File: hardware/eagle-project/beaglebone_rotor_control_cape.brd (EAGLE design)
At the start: 71.8 x 54.6 mm, 57 parts, among them IC1 TLC2264CDU, IC2 MCP4901, IC3 MAX3232ESE, IC4 TLC2264CDU, IC5 MCP4901, IC6 TLC2264CDU, Q1 SQ2348ES-T1-GE3, Q2 SQ2348ES-T1-GE3, Q3 SQ2348ES-T1-GE3, Q4 SQ2348ES-T1-GE3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

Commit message: * layout: added spi1 and determined pin for usb slave turn on
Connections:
- removed net N$23: R25.1
- removed net N$24: R24.1
- removed net N$26: R23.1
- new net BB_SPI1_CS0: R25.1, X1.74
- new net BB_SPI1_D0: R23.1, X1.75
- new net BB_SPI1_D1: X1.76
- new net BB_SPI1_SCLK: R24.1, X1.77
- new net BB_USB_VCC: X1.18
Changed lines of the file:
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@@
 <contactref element="R21" pad="1"/>
-</signal>
-<signal name="N$23">
-<contactref element="R25" pad="1"/>
-</signal>
-<signal name="N$24">
-<contactref element="R24" pad="1"/>
-</signal>
-<signal name="N$26">
-<contactref element="R23" pad="1"/>
 </signal>
 <signal name="N$27">
@@
 <contactref element="Q3" pad="3"/>
 </signal>
+<signal name="BB_USB_VCC">
+<contactref element="X1" pad="18"/>
+</signal>
+<signal name="BB_SPI1_CS0">
+<contactref element="X1" pad="74"/>
+<contactref element="R25" pad="1"/>
+<wire x1="-20.635" y1="-287.02" x2="35.56" y2="51.435" width="0" layer="19" extent="1-1"/>
+</signal>
+<signal name="BB_SPI1_SCLK">
+<contactref element="X1" pad="77"/>
+<contactref element="R24" pad="1"/>
+<wire x1="-20.635" y1="-280.67" x2="30.48" y2="53.975" width="0" layer="19" extent="1-1"/>
+</signal>
+<signal name="BB_SPI1_D1">
+<contactref element="X1" pad="76"/>
+</signal>
+<signal name="BB_SPI1_D0">
+<contactref element="X1" pad="75"/>
+<contactref element="R23" pad="1"/>
+<wire x1="-20.635" y1="-274.32" x2="33.02" y2="53.975" width="0" layer="19" extent="1-1"/>
+</signal>
 </signals>

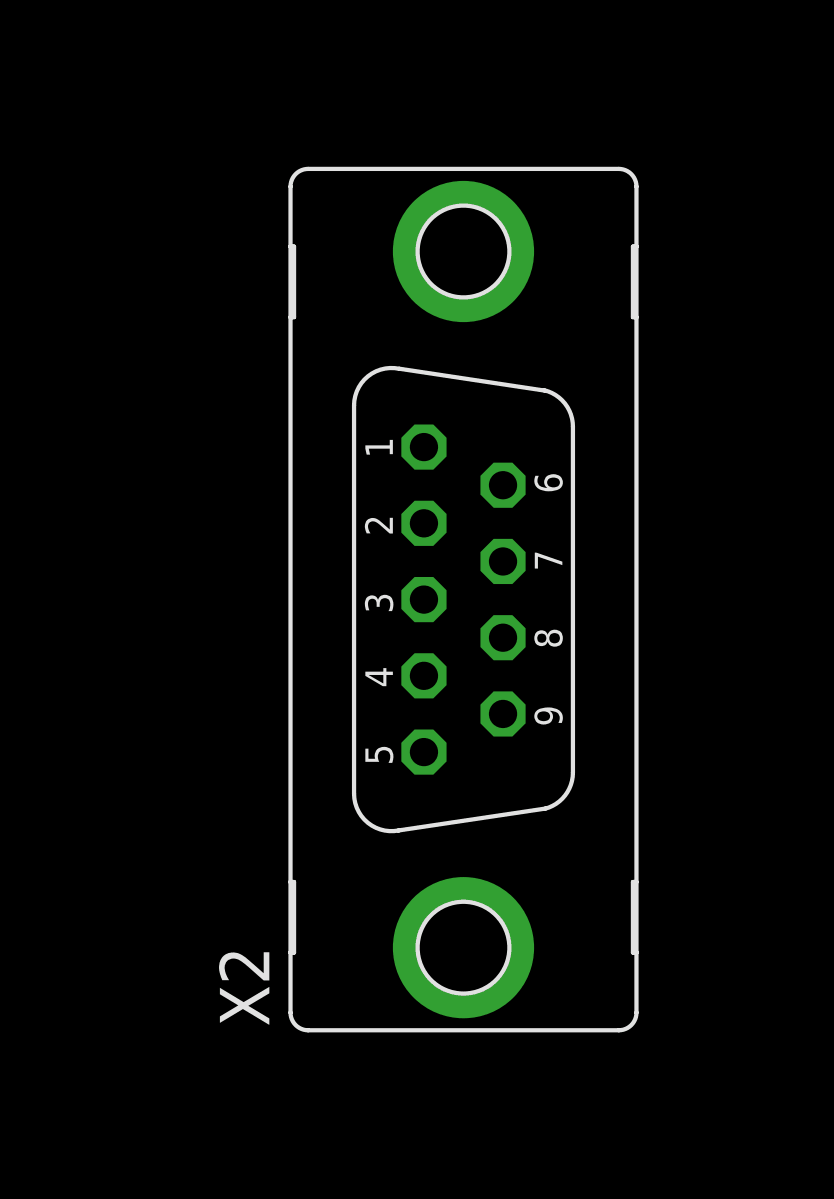
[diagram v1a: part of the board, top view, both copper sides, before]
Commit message: Created library for D-Sub connector from TE.com
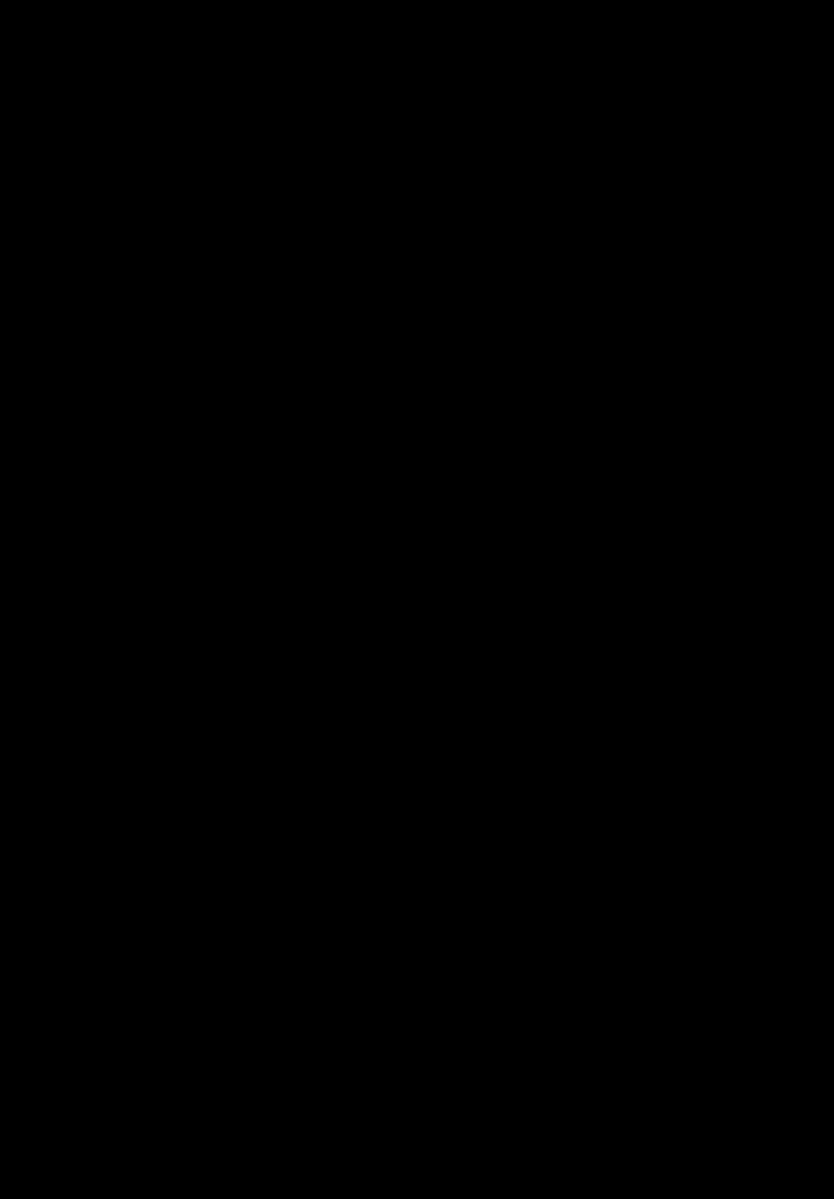
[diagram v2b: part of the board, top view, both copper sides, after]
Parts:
- removed X2: (no value), con-subd:F09VP
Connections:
- net GND: no longer X2.5
- net RS232_RX: no longer X2.3
- net RS232_TX: no longer X2.2
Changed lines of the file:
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@@
 <element name="R8" library="rcl" package="R0805" value="100" x="61.595" y="43.18" rot="R270"/>
 <element name="R1" library="rcl" package="R0805" value="100" x="59.055" y="43.18" rot="R270"/>
-<element name="X2" library="con-subd" package="F09VP" value="" x="6.35" y="-123.19" rot="R90">
-<attribute name="OC_NEWARK" value="unknown" x="6.35" y="-123.19" size="1.778" layer="27" rot="R90" display="off"/>
-<attribute name="MPN" value="" x="6.35" y="-123.19" size="1.778" layer="27" rot="R90" display="off"/>
-<attribute name="MF" value="" x="6.35" y="-123.19" size="1.778" layer="27" rot="R90" display="off"/>
-<attribute name="OC_FARNELL" value="unknown" x="6.35" y="-123.19" size="1.778" layer="27" rot="R90" display="off"/>
-</element>
 <element name="R10" library="rcl" package="R0805" value="10k" x="-11.43" y="-148.59"/>
 <element name="D1" library="diode" package="SOT23" value="BAS40-04" x="-11.43" y="-156.21"/>
@@
 <contactref element="IC3" pad="15"/>
 <contactref element="C6" pad="2"/>
-<contactref element="X2" pad="5"/>
 <contactref element="C7" pad="2"/>
 <contactref element="IC2" pad="7"/>
@@
 <wire x1="-12.38" y1="-164.93" x2="-18.415" y2="-184.725" width="0" layer="19" extent="1-1"/>
 <wire x1="-12.38" y1="-157.31" x2="-12.38" y2="-164.93" width="0" layer="19" extent="1-1"/>
-<wire x1="4.9276" y1="-128.6764" x2="-12.38" y2="-157.31" width="0" layer="19" extent="1-1"/>
-<wire x1="1.27" y1="-74.87" x2="4.9276" y2="-128.6764" width="0" layer="19" extent="1-1"/>
-<wire x1="-3.49" y1="-69.85" x2="1.27" y2="-74.87" width="0" layer="19" extent="1-1"/>
-<wire x1="-3.49" y1="-58.42" x2="-3.49" y2="-69.85" width="0" layer="19" extent="1-1"/>
-<wire x1="-1.59" y1="-51.9" x2="-3.49" y2="-58.42" width="0" layer="19" extent="1-1"/>
-<wire x1="-1.59" y1="-44.28" x2="-1.59" y2="-51.9" width="0" layer="19" extent="1-1"/>
-<wire x1="-1.69" y1="-38.1" x2="-1.59" y2="-44.28" width="0" layer="19" extent="1-1"/>
-<wire x1="-3.49" y1="-34.29" x2="-1.69" y2="-38.1" width="0" layer="19" extent="1-1"/>
 <wire x1="-11.11" y1="-309.075" x2="-14.92" y2="-236.22" width="0" layer="19" extent="1-1"/>
 <wire x1="-8.04" y1="-314.325" x2="-11.11" y2="-309.075" width="0" layer="19" extent="1-1"/>
@@
 <wire x1="-20.635" y1="-336.55" x2="-18.735" y2="-330.665" width="0" layer="19" extent="1-1"/>
 <wire x1="-14.92" y1="-336.55" x2="-20.635" y2="-336.55" width="0" layer="19" extent="1-1"/>
+<wire x1="1.27" y1="-74.87" x2="-12.38" y2="-157.31" width="0" layer="19" extent="1-1"/>
+<wire x1="-3.49" y1="-69.85" x2="1.27" y2="-74.87" width="0" layer="19" extent="1-1"/>
+<wire x1="-3.49" y1="-58.42" x2="-3.49" y2="-69.85" width="0" layer="19" extent="1-1"/>
+<wire x1="-1.59" y1="-51.9" x2="-3.49" y2="-58.42" width="0" layer="19" extent="1-1"/>
+<wire x1="-1.59" y1="-44.28" x2="-1.59" y2="-51.9" width="0" layer="19" extent="1-1"/>
+<wire x1="-1.69" y1="-38.1" x2="-1.59" y2="-44.28" width="0" layer="19" extent="1-1"/>
+<wire x1="-3.49" y1="-34.29" x2="-1.69" y2="-38.1" width="0" layer="19" extent="1-1"/>
 <wire x1="68.58" y1="3.175" x2="-3.49" y2="-34.29" width="0" layer="19" extent="1-1"/>
 <wire x1="68.58" y1="5.715" x2="68.58" y2="3.175" width="0" layer="19" extent="1-1"/>
@@
 <signal name="RS232_TX">
 <contactref element="IC3" pad="14"/>
-<contactref element="X2" pad="2"/>
-<wire x1="57.15" y1="38.6334" x2="4.9276" y2="-120.4468" width="0" layer="19" extent="1-1"/>
 </signal>
 <signal name="RS232_RX">
 <contactref element="IC3" pad="13"/>
-<contactref element="X2" pad="3"/>
-<wire x1="58.42" y1="38.6334" x2="4.9276" y2="-123.19" width="0" layer="19" extent="1-1"/>
 </signal>
 <signal name="ROT_H_POSITON">

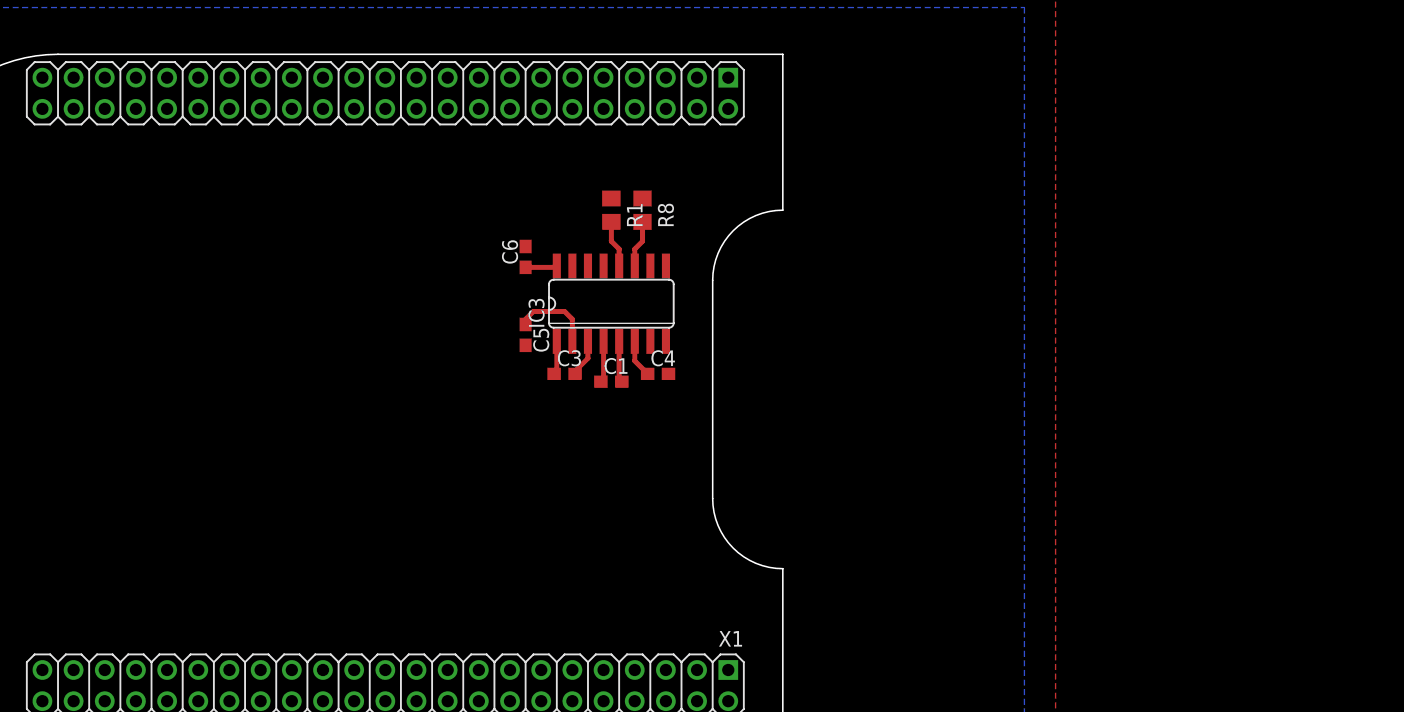
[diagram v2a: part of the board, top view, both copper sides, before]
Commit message: Placed D-Sub connectors on layout
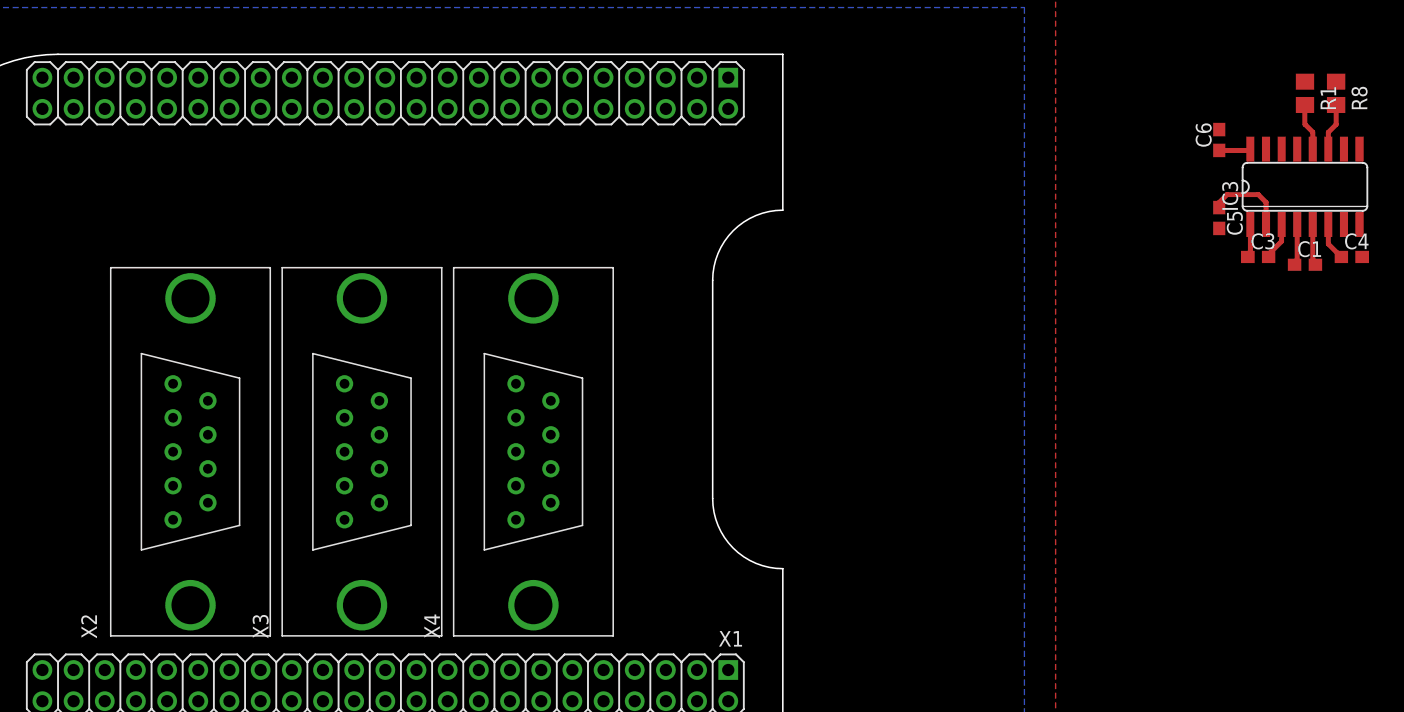
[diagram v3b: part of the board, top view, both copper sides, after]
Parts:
- added X2, X3, X4: DSUB9, con-te-dsub:DSUB9
- moved C3 57.3 mm to (111.8, 39.4)
- moved R8 57.3 mm to (118.1, 52.7)
- moved C1 57.3 mm to (115.6, 38.7)
- moved C4 57.3 mm to (119.4, 39.4)
- moved C5 57.3 mm to (108.6, 42.5)
- moved C6 57.3 mm to (108.6, 48.9)
- moved IC3 57.3 mm to (115.6, 45.1)
- moved R1 57.3 mm to (115.6, 52.7)
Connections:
- net GND: now also X3.6, X3.7, X3.8, X3.9, X4.6, X4.7, X4.8, X4.9
- net ROT_E_DOWN: now also X4.2
- net ROT_E_POSITION: now also X4.5
- net ROT_E_SPEED: now also X4.4
- net ROT_E_UP: now also X4.1
- net ROT_H_LEFT: now also X3.1
- net ROT_H_POSITON: now also X3.5
- net ROT_H_RIGHT: now also X3.2
- net ROT_H_SPEED: now also X3.4

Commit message: Added USB connector
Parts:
- added X5: USBDEV, con-usbbuchse:USB
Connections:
- net GND: now also X5.GND
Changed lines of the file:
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@@
 <element name="X3" library="con-te-dsub" package="DSUB9" value="DSUB9" x="38.735" y="23.495" rot="R90"/>
 <element name="X4" library="con-te-dsub" package="DSUB9" value="DSUB9" x="52.705" y="23.495" rot="R90"/>
+<element name="X5" library="con-usbbuchse" package="USB" value="USBDEV" x="-13.335" y="-349.885"/>
 </elements>
 <signals>
@@
 <contactref element="X4" pad="8"/>
 <contactref element="X4" pad="9"/>
+<contactref element="X5" pad="GND"/>
 <wire x1="-8.04" y1="-235.585" x2="-14.92" y2="-236.22" width="0" layer="19" extent="1-1"/>
 <wire x1="-7.935" y1="-227.965" x2="-8.04" y2="-235.585" width="0" layer="19" extent="1-1"/>
@@
 <wire x1="-20.635" y1="-336.55" x2="-18.735" y2="-330.665" width="0" layer="19" extent="1-1"/>
 <wire x1="-14.92" y1="-336.55" x2="-20.635" y2="-336.55" width="0" layer="19" extent="1-1"/>
+<wire x1="-9.835" y1="-347.175" x2="-14.92" y2="-336.55" width="0" layer="19" extent="1-1"/>
 <wire x1="1.27" y1="-74.87" x2="-12.38" y2="-157.31" width="0" layer="19" extent="1-1"/>
 <wire x1="-3.49" y1="-69.85" x2="1.27" y2="-74.87" width="0" layer="19" extent="1-1"/>
@@
 <wire x1="-3.49" y1="-34.29" x2="-1.69" y2="-38.1" width="0" layer="19" extent="1-1"/>
 <wire x1="40.155" y1="19.34" x2="-3.49" y2="-34.29" width="0" layer="19" extent="1-1"/>
+<wire x1="40.155" y1="22.11" x2="40.155" y2="19.34" width="0" layer="19" extent="1-1"/>
+<wire x1="40.155" y1="24.88" x2="40.155" y2="22.11" width="0" layer="19" extent="1-1"/>
+<wire x1="40.155" y1="27.65" x2="40.155" y2="24.88" width="0" layer="19" extent="1-1"/>
+<wire x1="54.125" y1="27.65" x2="40.155" y2="27.65" width="0" layer="19" extent="1-1"/>
+<wire x1="54.125" y1="24.88" x2="54.125" y2="27.65" width="0" layer="19" extent="1-1"/>
+<wire x1="54.125" y1="22.11" x2="54.125" y2="24.88" width="0" layer="19" extent="1-1"/>
+<wire x1="54.125" y1="19.34" x2="54.125" y2="22.11" width="0" layer="19" extent="1-1"/>
+<wire x1="68.58" y1="5.715" x2="54.125" y2="19.34" width="0" layer="19" extent="1-1"/>
+<wire x1="68.58" y1="3.175" x2="68.58" y2="5.715" width="0" layer="19" extent="1-1"/>
+<wire x1="68.58" y1="51.435" x2="54.125" y2="27.65" width="0" layer="19" extent="1-1"/>
+<wire x1="68.58" y1="53.975" x2="68.58" y2="51.435" width="0" layer="19" extent="1-1"/>
+<wire x1="15.24" y1="51.435" x2="40.155" y2="27.65" width="0" layer="19" extent="1-1"/>
+<wire x1="15.24" y1="53.975" x2="15.24" y2="51.435" width="0" layer="19" extent="1-1"/>
+<wire x1="12.7" y1="53.975" x2="15.24" y2="53.975" width="0" layer="19" extent="1-1"/>
+<wire x1="12.7" y1="51.435" x2="15.24" y2="51.435" width="0" layer="19" extent="1-1"/>
 <wire x1="108.585" y1="49.745" x2="68.58" y2="51.435" width="0" layer="19" extent="1-1"/>
 <wire x1="112.395" y1="48.1584" x2="108.585" y2="49.745" width="0" layer="19" extent="1-1"/>

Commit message: Updated schematic
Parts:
- moved X5 368.1 mm to (77.1, 6.99), turned to 90 degrees
- moved R8 67.6 mm to (52.1, 38.1), flipped to the bottom, turned to 180 degrees
- moved R1 64.6 mm to (52.1, 40.6), flipped to the bottom, turned to 180 degrees
- moved IC3 56.1 mm to (59.7, 40.6), flipped to the bottom, turned to 270 degrees
- moved C4 54.0 mm to (65.4, 36.8), flipped to the bottom, turned to 270 degrees
- moved C6 52.7 mm to (55.9, 47.6), flipped to the bottom, turned to 0 degrees
- moved C1 49.6 mm to (66.0, 40.6), flipped to the bottom, turned to 270 degrees
- moved X2 47.8 mm to (72.4, 27.9), turned to 270 degrees
- moved C3 46.6 mm to (65.4, 44.5), flipped to the bottom, turned to 270 degrees
- moved C5 46.6 mm to (62.2, 47.6), flipped to the bottom, turned to 180 degrees
- moved X3 15.3 mm to (23.5, 22.9)
- moved X4 15.3 mm to (37.5, 22.9)
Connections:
- removed net BB_AIN1: C2.1, R4.1, R5.2
- removed net BB_AIN2: C9.1, R26.1, R27.2
- removed net N$14: R7.1
- removed net N$15: R6.1
- removed net N$34: R31.1
- removed net N$37: R32.1
- new net BB_AIN_E: C9.1, R26.1, R27.2, X1.84
- new net BB_AIN_H: C2.1, R4.1, R5.2, X1.82
- new net BB_DOUT_DOWN: R31.1, X1.17
- new net BB_DOUT_LEFT: R6.1, X1.11
- new net BB_DOUT_RIGHT: R7.1, X1.13
- new net BB_DOUT_UP: R32.1, X1.15
- new net N$41: X1.19
- new net N$42: X1.16
- new net N$43: X1.14
- new net N$44: X1.12

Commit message: Updated eagle schematic
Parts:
- removed X4: DSUB9, con-te-dsub:DSUB9
- added Q5: SQ2348ES-T1-GE3, vishay_sq2348eS-t1-ge3:SOT23
- added R33: 1M, rcl:R0805
- added R34: 100, rcl:R0805
- moved R21 232.4 mm to (79.5, -51.5)
- moved R20 224.7 mm to (74.0, -51.0)
- moved R19 221.2 mm to (74.0, -48.5)
- moved R18 218.2 mm to (74.0, -45.5)
- moved R13 193.7 mm to (87.0, -46.0), turned to 90 degrees
- moved R12 191.8 mm to (90.0, -44.0), turned to 90 degrees
- moved R11 175.6 mm to (83.0, -52.5), turned to 90 degrees
- moved IC2 171.3 mm to (80.5, -47.0), turned to 270 degrees
- moved R9 166.7 mm to (90.0, -39.0), turned to 90 degrees
- moved D2 162.2 mm to (84.5, -33.0), turned to 180 degrees
- moved R7 159.0 mm to (91.5, -56.5)
- moved R6 158.8 mm to (82.5, -56.0)
- moved D1 158.3 mm to (88.0, -33.0), turned to 180 degrees
- moved R10 152.6 mm to (91.0, -35.5)
- moved X2 109.0 mm to (-36.6, 26.4)
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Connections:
- new net N$14: Q5.3, X5.GND
- new net N$23: Q5.1, R33.2, R34.2
- new net N$24: R34.1
- net +5V: now also X5.1-VCC
- net GND: now also Q5.2, R33.1; no longer X3.6, X3.7, X3.8, X3.9, X4.6, X4.7, X4.8, X4.9, X5.GND
- net N$2: now also IC1.12; no longer IC1.3
- net N$3: now also IC1.14; no longer IC1.1
- net N$5: now also IC1.13; no longer IC1.2
- net ROT_E_DOWN: no longer X4.2
- net ROT_E_POSITION: now also X3.1; no longer X4.5
- net ROT_E_SPEED: no longer X4.4
- net ROT_E_UP: no longer X4.1
- net ROT_H_LEFT: now also X3.3; no longer X3.1
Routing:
- net +3V3: track 2.59 -> 31.2 mm, vias 0 -> 1
- net +5V: track 0.00 -> 25.8 mm, vias 0 -> 2
- net ROT_H_LEFT: track 0.00 -> 18.5 mm
- net BB_DOUT_RIGHT: track 0.00 -> 18.4 mm
- net GND: track 0.00 -> 15.1 mm, vias 0 -> 2
- net ROT_H_RIGHT: track 0.00 -> 11.6 mm
- net ROT_H_SPEED: track 0.00 -> 10.7 mm
- net N$12: track 0.00 -> 10.6 mm
- net ROT_H_POSITON: track 0.00 -> 8.85 mm
- net BB_DOUT_LEFT: track 0.00 -> 8.05 mm
- net N$13: track 0.00 -> 7.18 mm
- net N$5: track 0.00 -> 6.41 mm
- net N$3: track 0.00 -> 5.68 mm
- net N$7: track 0.00 -> 5.26 mm
- net BB_AIN_H: track 0.00 -> 5.11 mm
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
